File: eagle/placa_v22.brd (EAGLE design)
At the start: 100 x 80 mm, 33 parts, among them IC1 7805, Q1 IRF740, Y1 16MHz

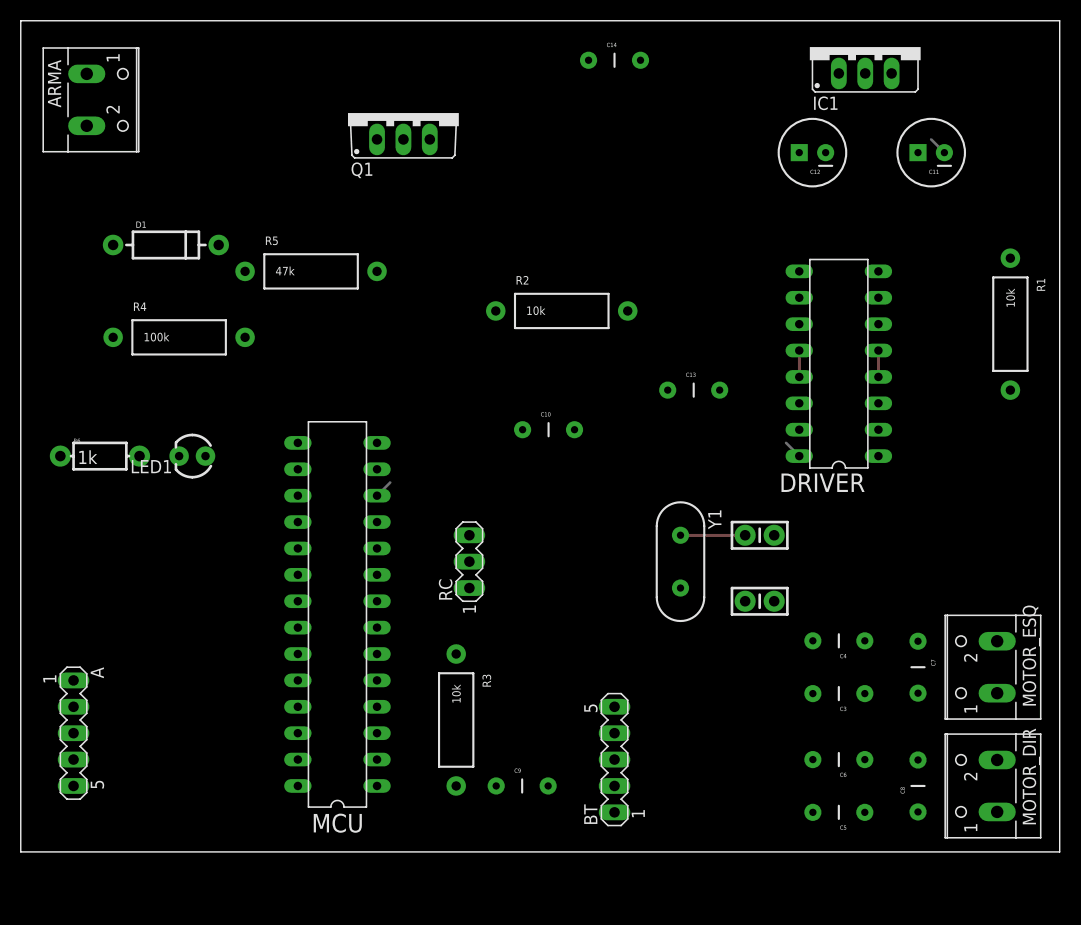
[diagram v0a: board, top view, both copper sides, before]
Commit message: Nova classe ConfigSensor pra armazenar na EEPROM. Ajustes no circuito e placa.
git-svn-id: https://mbs-bot.googlecode.com/svn/trunk@216 3c29fe3e-da84-11de-ae71-c59d11f48c9c
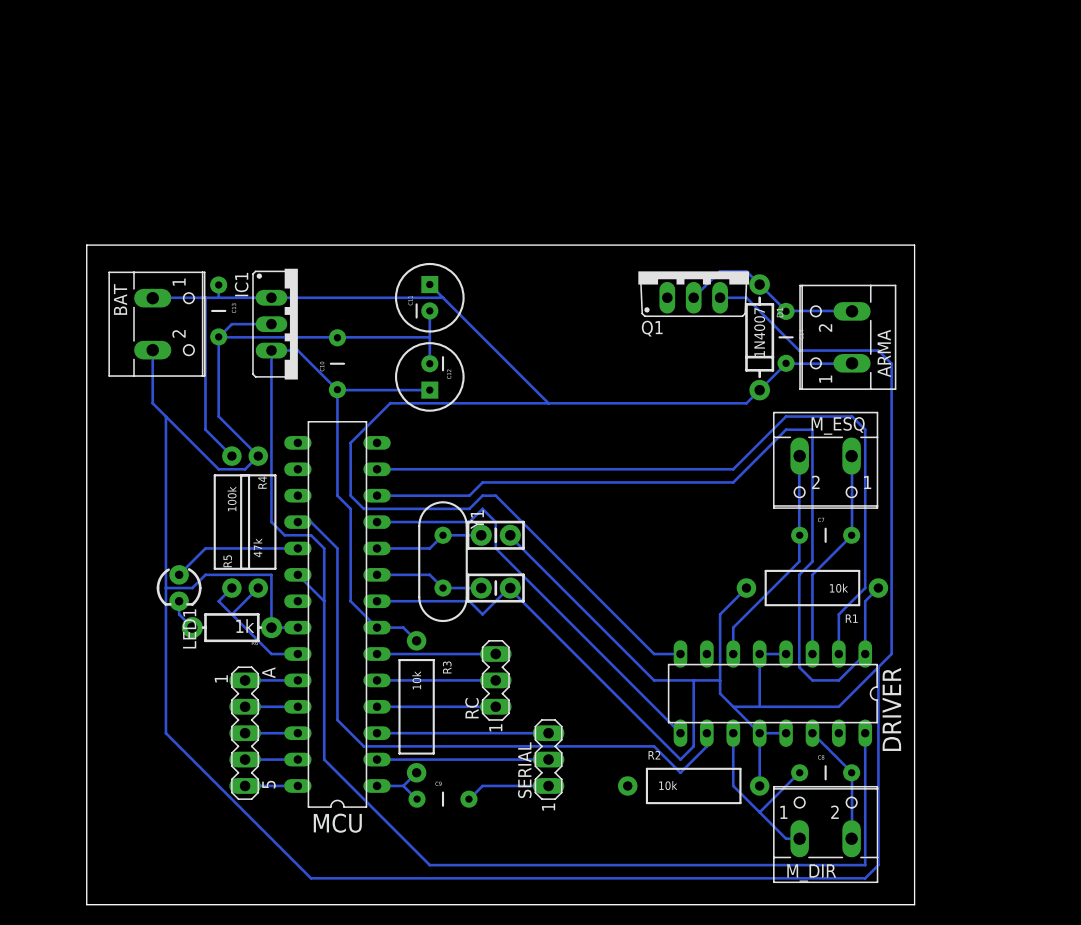
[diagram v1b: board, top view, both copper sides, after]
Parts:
- removed BT: (no value), con-lstb:MA05-1
- removed C3, C4, C5, C6: 100n, SparkFun:CAP-PTH-5MM
- removed MOTOR_DIR, MOTOR_ESQ: (no value), con-wago-500:W237-102
- added BAT: 12V, con-wago-500:W237-102
- added M_DIR, M_ESQ: (no value), con-wago-500:W237-102
- added SERIAL: TTL, con-lstb:MA03-1
- D1: value (none) -> 1N4007
- LED1: value (none) -> 3mm
- moved ARMA 74.7 mm to (78.7, 49.5), turned to 90 degrees
- moved IC1 60.8 mm to (26.7, 50.8), turned to 270 degrees
- moved D1 57.8 mm to (71.1, 49.5), turned to 270 degrees
- moved C11 50.2 mm to (39.4, 53.3), turned to 90 degrees
- moved R2 47.5 mm to (64.8, 6.35)
- moved C13 46.4 mm to (19.1, 52.1), turned to 270 degrees
- moved C12 42.7 mm to (39.4, 45.7), turned to 270 degrees
- moved DRIVER 33.9 mm to (71.1, 15.2), turned to 180 degrees
- moved Q1 31.8 mm to (64.8, 55.9)
- moved R1 31.8 mm to (76.2, 25.4), turned to 180 degrees
- moved C14 31.4 mm to (73.7, 49.5), turned to 270 degrees
- moved C1 25.4 mm to (45.7, 25.4)
- moved C2 25.4 mm to (45.7, 30.5)
- moved R5 24.7 mm to (22.9, 31.8), turned to 90 degrees
- moved Y1 22.9 mm to (40.6, 27.9)
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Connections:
- removed net D9: DRIVER.15, MCU.15, MCU.16, Q1.G
- new net N$17: MCU.16, Q1.G
- new net N$19: DRIVER.15, MCU.15
- net +5V: no longer BT.2
- net A: now also SERIAL.2; no longer BT.4
- net GND: now also BAT.2; no longer BT.1, C3.2, C4.2, C5.2, C6.2
- net N$10: now also SERIAL.1; no longer BT.3
- net N$5: now also C7.2, M_ESQ.1; no longer C4.1, C7.1, MOTOR_ESQ.2
- net N$6: now also C7.1, M_ESQ.2; no longer C3.1, C7.2, MOTOR_ESQ.1
- net N$7: now also M_DIR.1; no longer C5.1, MOTOR_DIR.1
- net N$8: now also M_DIR.2; no longer C6.1, MOTOR_DIR.2
- net N$9: now also SERIAL.3; no longer BT.5
- net VCC: now also BAT.1
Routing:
- net GND: track 6.88 -> 373.7 mm
- net +5V: track 1.84 -> 161.2 mm
- net VCC: track 0.00 -> 157.4 mm
- net D6: track 1.80 -> 82.7 mm
- net D7: track 0.00 -> 72.3 mm
- net D12: track 0.00 -> 61.4 mm
- net D5: track 0.00 -> 40.2 mm
- net N$6: track 0.00 -> 21.8 mm
- net N$5: track 0.00 -> 20.7 mm
- net N$7: track 0.00 -> 19.0 mm
- net N$11: track 0.00 -> 18.0 mm
- net N$9: track 0.00 -> 16.5 mm
- net A: track 0.00 -> 16.5 mm
- net A0: track 0.00 -> 15.1 mm
- net D13: track 0.00 -> 12.5 mm
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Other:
- board size 100 x 80 mm -> 79.7 x 63.5 mm
